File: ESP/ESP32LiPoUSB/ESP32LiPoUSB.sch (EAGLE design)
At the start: 25 parts, among them Q1 mmbt2222, Q2 mmbt2222, Q3 DMG3415U, SW2 KMR2, X1 JSTPH, X2 ESP32_WROOM32_SKINNY

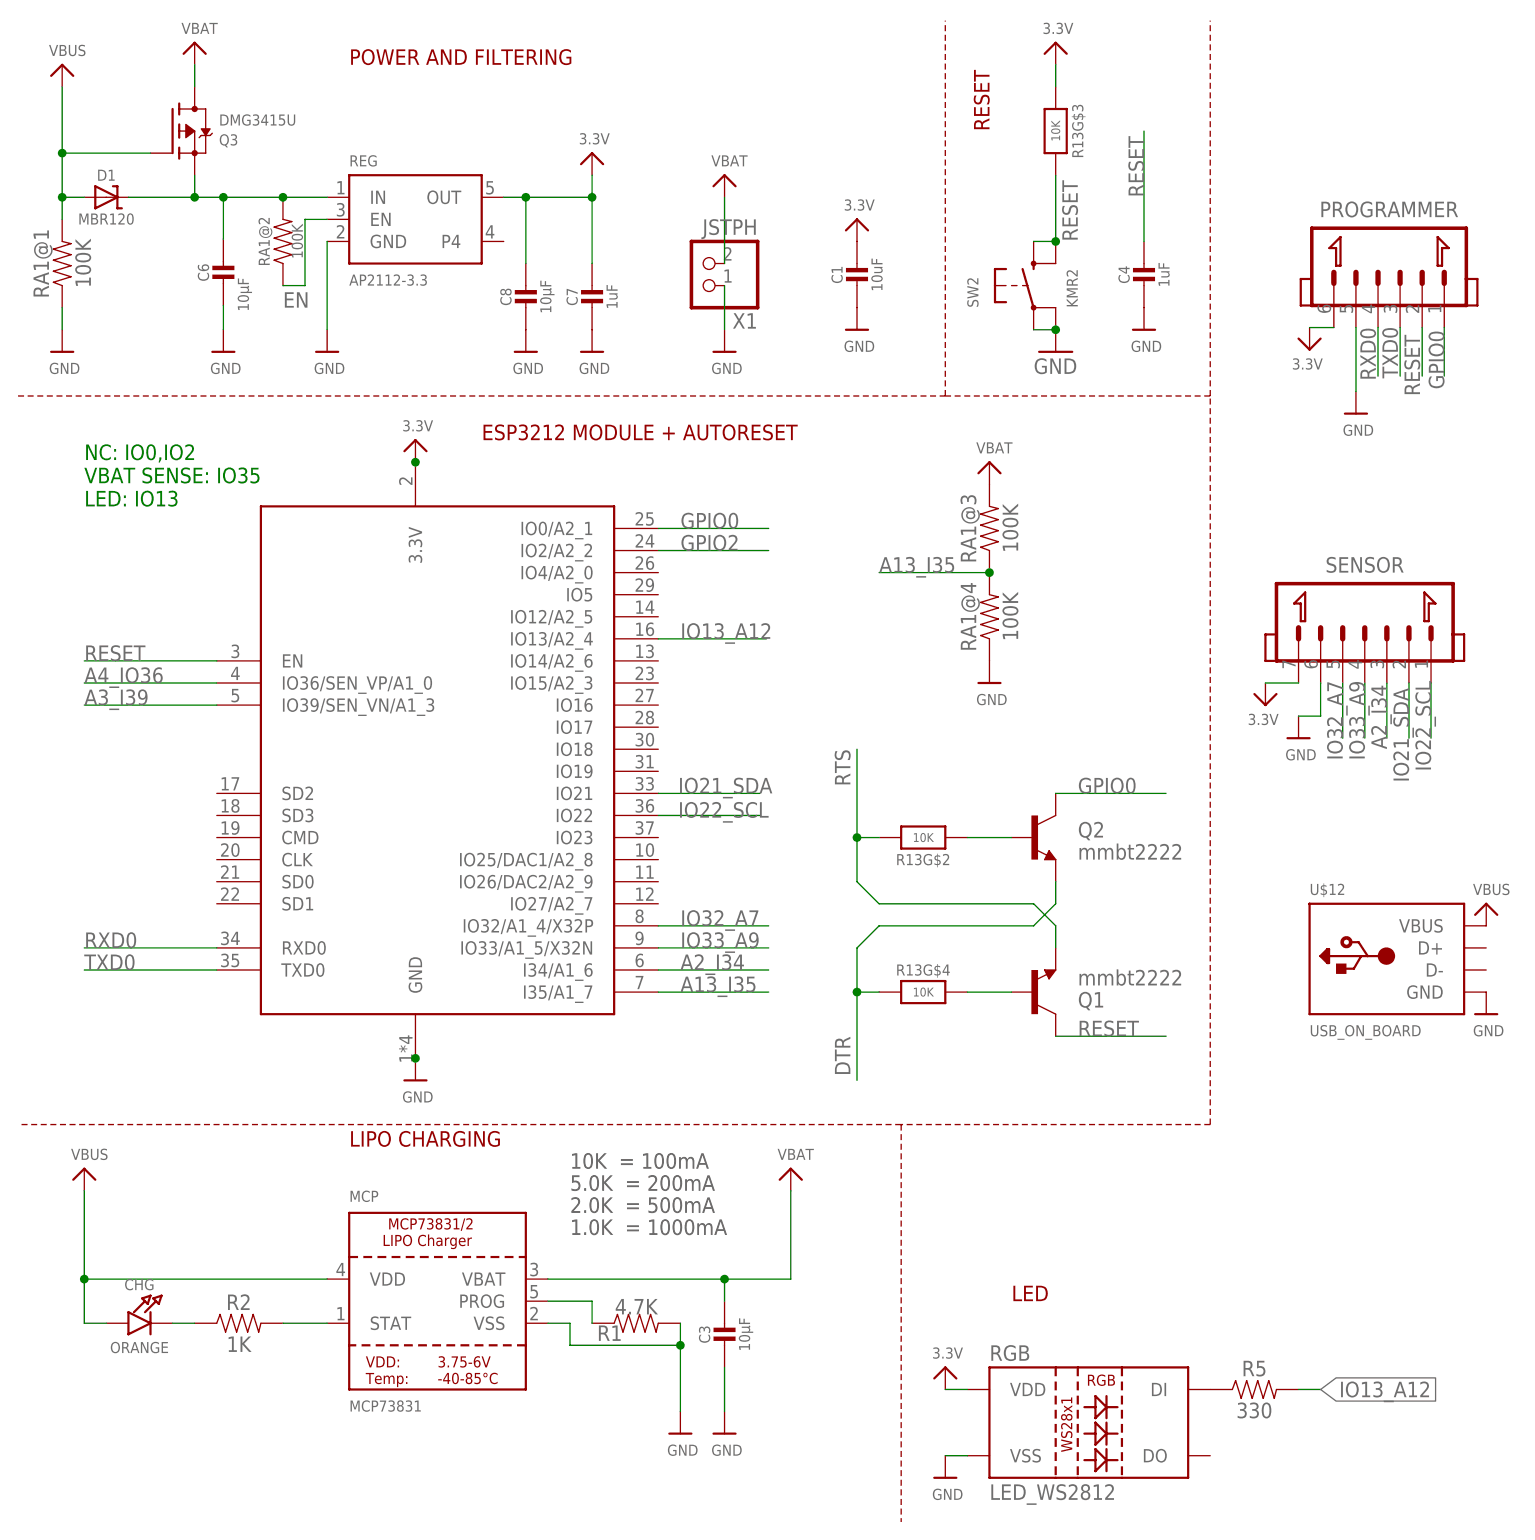
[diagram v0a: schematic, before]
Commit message: take out autoprgm
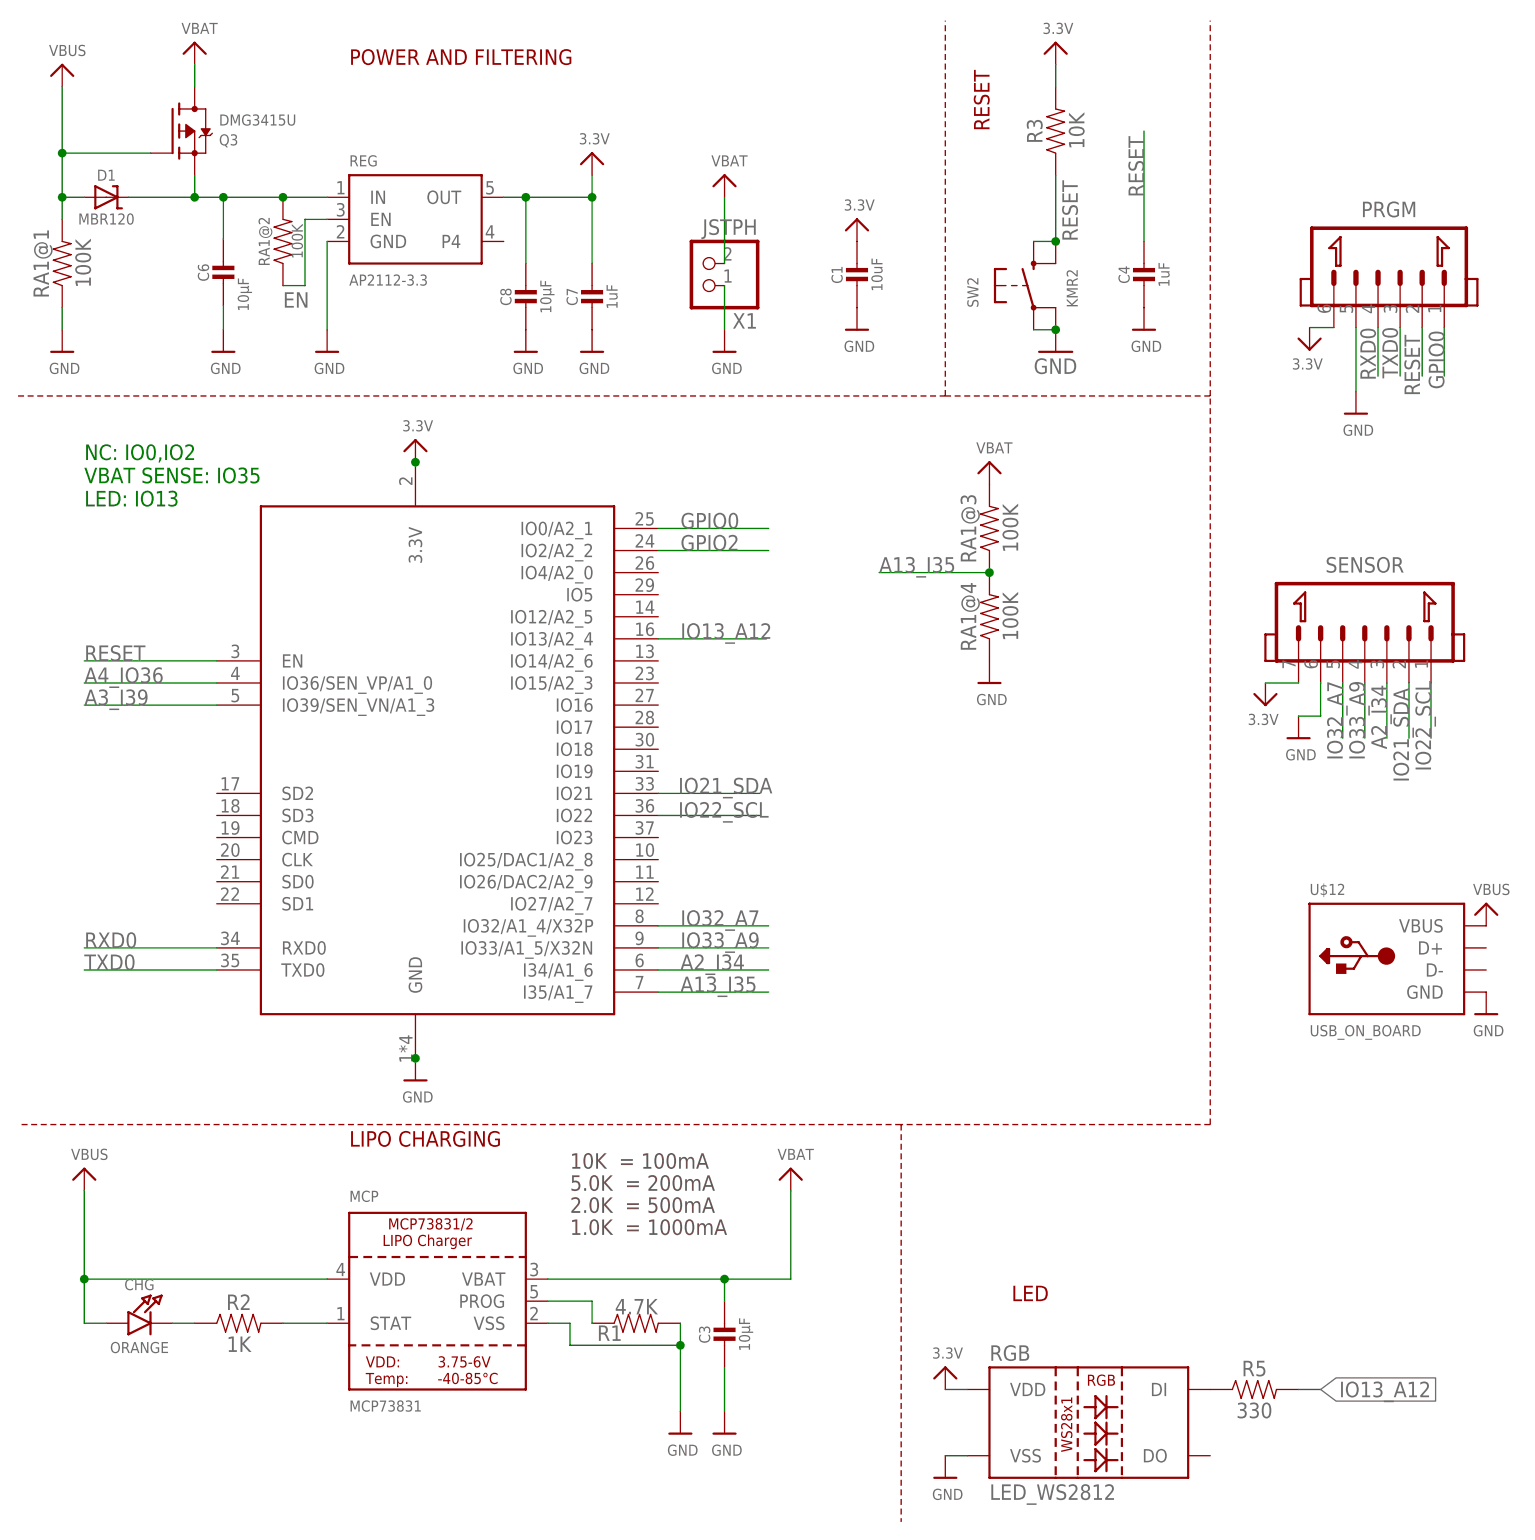
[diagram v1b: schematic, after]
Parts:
- removed Q1, Q2: mmbt2222, SparkFun:TRANSISTOR_NPNSOT23-3
- removed R13: 10K, microbuilder:RESISTOR_4PACK
- added R3: 10K, Scott-Electrical:RESISTOR0603
- renumbered PROGRAMMER to PRGM
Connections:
- removed net DTR: Q2.E, R13G$4.1
- removed net N$12: Q1.B, R13G$4.2
- removed net N$13: Q2.B, R13G$2.1
- removed net RTS: Q1.E, R13G$2.2
- net 3.3V: now also R3.2; no longer R13G$3.1
- net GPIO0: no longer Q2.C
- net RESET: now also R3.1; no longer Q1.C, R13G$3.2
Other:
- note removed: "ESP3212 MODULE + AUTORESET"
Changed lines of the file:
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@@
 <setting verticaltext="up"/>
 </settings>
-<grid distance="0.05" unitdist="inch" unit="inch" style="lines" multiple="1" display="no" altdistance="0.01" altunitdist="inch" altunit="inch"/>
+<grid distance="0.1" unitdist="inch" unit="inch" style="lines" multiple="1" display="no" altdistance="0.01" altunitdist="inch" altunit="inch"/>
 <layers>
 <layer number="1" name="Top" color="4" fill="1" visible="no" active="no"/>
@@
 <part name="GND6" library="supply1" deviceset="GND" device=""/>
 <part name="U$10" library="microbuilder" deviceset="3.3V" device=""/>
-<part name="Q1" library="SparkFun" deviceset="TRANSISTOR_NPN" device="SOT23-3" value="mmbt2222"/>
-<part name="Q2" library="SparkFun" deviceset="TRANSISTOR_NPN" device="SOT23-3" value="mmbt2222"/>
 <part name="U$26" library="microbuilder" deviceset="3.3V" device=""/>
 <part name="U$37" library="microbuilder" deviceset="GND" device=""/>
@@
 <part name="Q3" library="microbuilder" deviceset="MOSFET-P" device="" value="DMG3415U"/>
 <part name="U$25" library="microbuilder" deviceset="GND" device=""/>
-<part name="R13" library="microbuilder" deviceset="RESISTOR_4PACK" device="" value="10K"/>
 <part name="U$40" library="microbuilder" deviceset="VBAT" device=""/>
 <part name="U$41" library="microbuilder" deviceset="GND" device=""/>
@@
 <part name="RA1" library="Scott-Electrical" deviceset="RESISTOR_ARRAY_1206_SEPARATE" device="" value="100K"/>
 <part name="R1" library="Scott-Electrical" deviceset="RESISTOR" device="0603" package3d_urn="urn:adsk.eagle:package:39650/1" value="4.7K"/>
-<part name="PROGRAMMER" library="Scott-Connectors" deviceset="JST_1.25_6P" device=""/>
+<part name="PRGM" library="Scott-Connectors" deviceset="JST_1.25_6P" device=""/>
 <part name="U$1" library="microbuilder" deviceset="3.3V" device=""/>
 <part name="U$8" library="microbuilder" deviceset="GND" device=""/>
@@
 <part name="U$17" library="microbuilder" deviceset="GND" device=""/>
 <part name="U$18" library="microbuilder" deviceset="VBUS" device=""/>
+<part name="R3" library="Scott-Electrical" deviceset="RESISTOR" device="0603" package3d_urn="urn:adsk.eagle:package:39650/1" value="10K"/>
 </parts>
 <sheets>
@@
 <text x="43.18" y="45.72" size="1.778" layer="94">LIPO CHARGING</text>
 <text x="119.38" y="27.94" size="1.778" layer="94">LED</text>
-<text x="58.42" y="127" size="1.778" layer="94">ESP3212 MODULE + AUTORESET</text>
 <text x="12.7" y="119.38" size="1.778" layer="91">NC: IO0,IO2
 VBAT SENSE: IO35
@@
 <attribute name="VALUE" x="69.596" y="161.036" size="1.27" layer="96"/>
 </instance>
-<instance part="Q1" gate="G$1" x="121.92" y="63.5" smashed="yes" rot="MR180">
-<attribute name="NAME" x="127" y="63.5" size="1.778" layer="95" rot="MR180"/>
-<attribute name="VALUE" x="127" y="66.04" size="1.778" layer="96" rot="MR180"/>
-</instance>
-<instance part="Q2" gate="G$1" x="121.92" y="81.28" smashed="yes">
-<attribute name="NAME" x="127" y="81.28" size="1.778" layer="95"/>
-<attribute name="VALUE" x="127" y="78.74" size="1.778" layer="96"/>
-</instance>
 <instance part="U$26" gate="G$1" x="50.8" y="127" smashed="yes">
 <attribute name="VALUE" x="49.276" y="128.016" size="1.27" layer="96"/>
@@
 <attribute name="VALUE" x="8.636" y="134.62" size="1.27" layer="96"/>
 </instance>
-<instance part="R13" gate="G$3" x="124.46" y="162.56" smashed="yes" rot="R270">
-<attribute name="NAME" x="127" y="162.56" size="1.27" layer="95" font="vector" rot="R270" align="center"/>
-<attribute name="VALUE" x="124.46" y="162.56" size="1.016" layer="96" font="vector" ratio="15" rot="R270" align="center"/>
-</instance>
-<instance part="R13" gate="G$2" x="109.22" y="81.28" smashed="yes" rot="R180">
-<attribute name="NAME" x="109.22" y="78.74" size="1.27" layer="95" font="vector" rot="R180" align="center"/>
-<attribute name="VALUE" x="109.22" y="81.28" size="1.016" layer="96" font="vector" ratio="15" rot="R180" align="center"/>
-</instance>
-<instance part="R13" gate="G$4" x="109.22" y="63.5" smashed="yes">
-<attribute name="NAME" x="109.22" y="66.04" size="1.27" layer="95" font="vector" align="center"/>
-<attribute name="VALUE" x="109.22" y="63.5" size="1.016" layer="96" font="vector" ratio="15" align="center"/>
-</instance>
 <instance part="U$40" gate="G$1" x="116.84" y="124.46" smashed="yes">
 <attribute name="VALUE" x="115.316" y="125.476" size="1.27" layer="96"/>
@@
 <attribute name="VALUE" x="76.2" y="28.194" size="1.778" layer="96" font="vector" align="top-center"/>
 </instance>
-<instance part="PROGRAMMER" gate="&gt;NAME" x="162.814" y="150.114" smashed="yes" rot="R180">
+<instance part="PRGM" gate="&gt;NAME" x="162.814" y="150.114" smashed="yes" rot="R180">
 <attribute name="NAME" x="162.814" y="152.654" size="1.778" layer="95" font="vector" rot="R180" align="top-center"/>
 </instance>
@@
 <instance part="U$18" gate="G$1" x="173.99" y="73.66" smashed="yes">
 <attribute name="VALUE" x="172.466" y="74.676" size="1.27" layer="96"/>
+</instance>
+<instance part="R3" gate="G$1" x="124.46" y="162.56" smashed="yes" rot="R90">
+<attribute name="NAME" x="122.936" y="162.56" size="1.778" layer="95" font="vector" rot="R90" align="bottom-center"/>
+<attribute name="VALUE" x="125.984" y="162.56" size="1.778" layer="96" font="vector" rot="R90" align="top-center"/>
 </instance>
 </instances>
@@
 <segment>
 <pinref part="U$8" gate="G$1" pin="GND"/>
-<pinref part="PROGRAMMER" gate="&gt;NAME" pin="5"/>
+<pinref part="PRGM" gate="&gt;NAME" pin="5"/>
 <wire x1="159.004" y1="132.588" x2="159.004" y2="139.954" width="0.1524" layer="91"/>
 </segment>
@@
 <segment>
 <pinref part="U$5" gate="G$1" pin="3.3V"/>
-<pinref part="R13" gate="G$3" pin="1"/>
 <wire x1="124.46" y1="170.18" x2="124.46" y2="167.64" width="0.1524" layer="91"/>
+<pinref part="R3" gate="G$1" pin="2"/>
 </segment>
 <segment>
@@
 </segment>
 <segment>
-<pinref part="PROGRAMMER" gate="&gt;NAME" pin="6"/>
+<pinref part="PRGM" gate="&gt;NAME" pin="6"/>
 <pinref part="U$1" gate="G$1" pin="3.3V"/>
 <wire x1="153.67" y1="139.954" x2="156.464" y2="139.954" width="0.1524" layer="91"/>
@@
 <wire x1="124.46" y1="149.86" x2="121.92" y2="149.86" width="0.1524" layer="91"/>
 <junction x="124.46" y="149.86"/>
-<pinref part="R13" gate="G$3" pin="2"/>
-</segment>
-<segment>
-<wire x1="137.16" y1="58.42" x2="124.46" y2="58.42" width="0.1524" layer="91"/>
-<label x="127" y="58.42" size="1.778" layer="95"/>
-<pinref part="Q1" gate="G$1" pin="C"/>
+<pinref part="R3" gate="G$1" pin="1"/>
 </segment>
 <segment>
@@
 </segment>
 <segment>
-<pinref part="PROGRAMMER" gate="&gt;NAME" pin="2"/>
+<pinref part="PRGM" gate="&gt;NAME" pin="2"/>
 <wire x1="166.624" y1="139.954" x2="166.624" y2="134.366" width="0.1524" layer="91"/>
 <label x="166.37" y="132.08" size="1.778" layer="95" rot="R90"/>
@@
 </net>
 <net name="GPIO0" class="0">
-<segment>
-<wire x1="124.46" y1="86.36" x2="137.16" y2="86.36" width="0.1524" layer="91"/>
-<label x="127" y="86.36" size="1.778" layer="95"/>
-<pinref part="Q2" gate="G$1" pin="C"/>
-</segment>
 <segment>
 <wire x1="78.74" y1="116.84" x2="91.44" y2="116.84" width="0.1524" layer="91"/>
@@
 </segment>
 <segment>
-<pinref part="PROGRAMMER" gate="&gt;NAME" pin="1"/>
+<pinref part="PRGM" gate="&gt;NAME" pin="1"/>
 <wire x1="169.164" y1="139.954" x2="169.164" y2="134.366" width="0.1524" layer="91"/>
 <label x="169.164" y="132.842" size="1.778" layer="95" rot="R90"/>
@@
 </segment>
 <segment>
-<pinref part="PROGRAMMER" gate="&gt;NAME" pin="4"/>
+<pinref part="PRGM" gate="&gt;NAME" pin="4"/>
 <wire x1="161.544" y1="139.954" x2="161.544" y2="134.366" width="0.1524" layer="91"/>
 <label x="161.29" y="133.858" size="1.778" layer="95" rot="R90"/>
@@
 </segment>
 <segment>
-<pinref part="PROGRAMMER" gate="&gt;NAME" pin="3"/>
+<pinref part="PRGM" gate="&gt;NAME" pin="3"/>
 <wire x1="164.084" y1="139.954" x2="164.084" y2="134.366" width="0.1524" layer="91"/>
 <label x="163.83" y="134.112" size="1.778" layer="95" rot="R90"/>
 </segment>
 </net>
-<net name="RTS" class="0">
-<segment>
-<wire x1="124.46" y1="68.58" x2="124.46" y2="71.12" width="0.1524" layer="91"/>
-<wire x1="124.46" y1="71.12" x2="121.92" y2="73.66" width="0.1524" layer="91"/>
-<wire x1="121.92" y1="73.66" x2="104.14" y2="73.66" width="0.1524" layer="91"/>
-<wire x1="104.14" y1="73.66" x2="101.6" y2="76.2" width="0.1524" layer="91"/>
-<wire x1="101.6" y1="76.2" x2="101.6" y2="81.28" width="0.1524" layer="91"/>
-<wire x1="101.6" y1="81.28" x2="104.14" y2="81.28" width="0.1524" layer="91"/>
-<wire x1="101.6" y1="91.44" x2="101.6" y2="81.28" width="0.1524" layer="91"/>
-<junction x="101.6" y="81.28"/>
-<label x="99.06" y="91.44" size="1.778" layer="95" rot="R270"/>
-<pinref part="Q1" gate="G$1" pin="E"/>
-<pinref part="R13" gate="G$2" pin="2"/>
-</segment>
-</net>
-<net name="DTR" class="0">
-<segment>
-<wire x1="124.46" y1="76.2" x2="124.46" y2="73.66" width="0.1524" layer="91"/>
-<wire x1="124.46" y1="73.66" x2="121.92" y2="71.12" width="0.1524" layer="91"/>
-<wire x1="121.92" y1="71.12" x2="104.14" y2="71.12" width="0.1524" layer="91"/>
-<wire x1="104.14" y1="71.12" x2="101.6" y2="68.58" width="0.1524" layer="91"/>
-<wire x1="101.6" y1="68.58" x2="101.6" y2="63.5" width="0.1524" layer="91"/>
-<wire x1="101.6" y1="63.5" x2="104.14" y2="63.5" width="0.1524" layer="91"/>
-<wire x1="101.6" y1="63.5" x2="101.6" y2="53.34" width="0.1524" layer="91"/>
-<junction x="101.6" y="63.5"/>
-<label x="99.06" y="58.42" size="1.778" layer="95" rot="R270"/>
-<pinref part="Q2" gate="G$1" pin="E"/>
-<pinref part="R13" gate="G$4" pin="1"/>
-</segment>
-</net>
-<net name="N$12" class="0">
-<segment>
-<wire x1="119.38" y1="63.5" x2="114.3" y2="63.5" width="0.1524" layer="91"/>
-<pinref part="Q1" gate="G$1" pin="B"/>
-<pinref part="R13" gate="G$4" pin="2"/>
-</segment>
-</net>
-<net name="N$13" class="0">
-<segment>
-<wire x1="114.3" y1="81.28" x2="119.38" y2="81.28" width="0.1524" layer="91"/>
-<pinref part="Q2" gate="G$1" pin="B"/>
-<pinref part="R13" gate="G$2" pin="1"/>
-</segment>
-</net>
